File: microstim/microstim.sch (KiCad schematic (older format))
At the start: 89 parts, among them J1 Conn_Coaxial, J10 Conn_Coaxial, J11 Screw_Terminal_01x02, J12 Conn_Coaxial, J3 Screw_Terminal_01x02, J5 Conn_Coaxial, J7 Screw_Terminal_01x02, J9 Screw_Terminal_01x02, SW1 SW_Push, SW2 SW_Push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

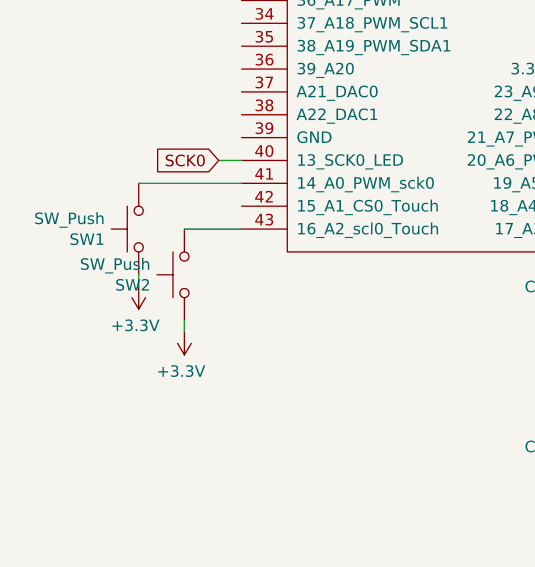
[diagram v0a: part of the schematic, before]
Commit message: added datasheets for connector and enclosure. updated BOM. probably tons of updates to schematic/layout (cant remember when last commit was). layout/schematic complete - just need double-checking.
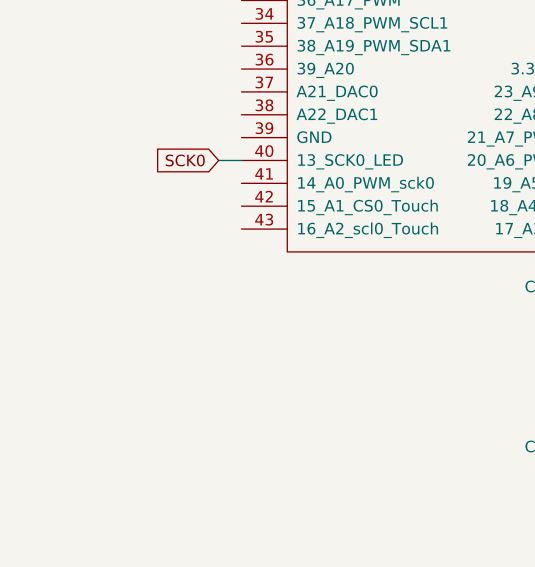
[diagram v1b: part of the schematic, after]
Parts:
- removed SW1, SW2: SW_Push, Button_Switch_SMD:SW_SPST_PTS645, symbol Switch:SW_Push
- J1, J10, J12, J5: footprint Connector_Coaxial:SMA_Amphenol_901-144_Vertical -> microstim:731375003
- J11, J3, J7, J9: footprint TerminalBlock_4Ucon:TerminalBlock_4Ucon_1x02_P3.50mm_Vertical -> microstim:1-2834016-2 _TERM_BLK_2P_SIDE_ENT_2.54MM_PCB
- U1: footprint microstim:Teensy35_36 -> microstim:Teensy35_36_noInternalPins
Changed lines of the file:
@@
 F 0 "U1" H 2150 5687 60  0000 C CNN
 F 1 "Teensy3.5" H 2150 5581 60  0000 C CNN
-F 2 "microstim:Teensy35_36" H 2150 3300 60  0001 C CNN
+F 2 "microstim:Teensy35_36_noInternalPins" H 2150 3300 60  0001 C CNN
 F 3 "" H 2150 3300 60  0000 C CNN
 	1    2150 3300
@@
 F 0 "J1" H 2480 6038 50  0000 C CNN
 F 1 "Conn_Coaxial" H 2480 5947 50  0000 C CNN
-F 2 "Connector_Coaxial:SMA_Amphenol_901-144_Vertical" H 2550 5800 50  0001 C CNN
+F 2 "microstim:731375003" H 2550 5800 50  0001 C CNN
 F 3 " ~" H 2550 5800 50  0001 C CNN
 	1    2550 5800
@@
 F 0 "J3" H 2820 6017 50  0000 C CNN
 F 1 "Screw_Terminal_01x02" H 2820 5926 50  0000 C CNN
-F 2 "TerminalBlock_4Ucon:TerminalBlock_4Ucon_1x02_P3.50mm_Vertical" H 2900 5800 50  0001 C CNN
+F 2 "microstim:1-2834016-2 _TERM_BLK_2P_SIDE_ENT_2.54MM_PCB" H 2900 5800 50  0001 C CNN
 F 3 "~" H 2900 5800 50  0001 C CNN
 	1    2900 5800
@@
 F 0 "J5" H 2480 6738 50  0000 C CNN
 F 1 "Conn_Coaxial" H 2480 6647 50  0000 C CNN
-F 2 "Connector_Coaxial:SMA_Amphenol_901-144_Vertical" H 2550 6500 50  0001 C CNN
+F 2 "microstim:731375003" H 2550 6500 50  0001 C CNN
 F 3 " ~" H 2550 6500 50  0001 C CNN
 	1    2550 6500
@@
 F 0 "J7" H 2820 6717 50  0000 C CNN
 F 1 "Screw_Terminal_01x02" H 2820 6626 50  0000 C CNN
-F 2 "TerminalBlock_4Ucon:TerminalBlock_4Ucon_1x02_P3.50mm_Vertical" H 2900 6500 50  0001 C CNN
+F 2 "microstim:1-2834016-2 _TERM_BLK_2P_SIDE_ENT_2.54MM_PCB" H 2900 6500 50  0001 C CNN
 F 3 "~" H 2900 6500 50  0001 C CNN
 	1    2900 6500
@@
 Wire Wire Line
 	3300 6400 3300 6500
-$Comp
-L Switch:SW_Push SW1
-U 1 1 5B7C9AA6
-P 700 5400
-F 0 "SW1" V 654 5548 50  0000 L CNN
-F 1 "SW_Push" V 745 5548 50  0000 L CNN
-F 2 "Button_Switch_SMD:SW_SPST_PTS645" H 700 5600 50  0001 C CNN
-F 3 "" H 700 5600 50  0001 C CNN
-	1    700  5400
-	0    -1   -1   0
-$EndComp
-$Comp
-L Switch:SW_Push SW2
-U 1 1 5B7C9D93
-P 900 5600
-F 0 "SW2" V 854 5748 50  0000 L CNN
-F 1 "SW_Push" V 945 5748 50  0000 L CNN
-F 2 "Button_Switch_SMD:SW_SPST_PTS645" H 900 5800 50  0001 C CNN
-F 3 "" H 900 5800 50  0001 C CNN
-	1    900  5600
-	0    -1   -1   0
-$EndComp
 $Comp
 L power:GND #PWR018
@@
 	1    0    0    -1
 $EndComp
-$Comp
-L power:+3.3V #PWR01
-U 1 1 5B7D4ED6
-P 700 5650
-F 0 "#PWR01" H 700 5500 50  0001 C CNN
-F 1 "+3.3V" H 715 5823 50  0000 C CNN
-F 2 "" H 700 5650 50  0001 C CNN
-F 3 "" H 700 5650 50  0001 C CNN
-	1    700  5650
-	-1   0    0    1
-$EndComp
-$Comp
-L power:+3.3V #PWR02
-U 1 1 5B7D4F09
-P 900 5850
-F 0 "#PWR02" H 900 5700 50  0001 C CNN
-F 1 "+3.3V" H 915 6023 50  0000 C CNN
-F 2 "" H 900 5850 50  0001 C CNN
-F 3 "" H 900 5850 50  0001 C CNN
-	1    900  5850
-	-1   0    0    1
-$EndComp
-Wire Wire Line
-	700  5600 700  5650
-Wire Wire Line
-	900  5800 900  5850
 $Comp
 L Device:R_US R3
@@
 F 0 "J12" H 15630 6038 50  0000 C CNN
 F 1 "Conn_Coaxial" H 15630 5947 50  0000 C CNN
-F 2 "Connector_Coaxial:SMA_Amphenol_901-144_Vertical" H 15700 5800 50  0001 C CNN
+F 2 "microstim:731375003" H 15700 5800 50  0001 C CNN
 F 3 " ~" H 15700 5800 50  0001 C CNN
 	1    15700 5800
@@
 F 0 "J11" H 15270 6017 50  0000 C CNN
 F 1 "Screw_Terminal_01x02" H 15270 5926 50  0000 C CNN
-F 2 "TerminalBlock_4Ucon:TerminalBlock_4Ucon_1x02_P3.50mm_Vertical" H 15350 5800 50  0001 C CNN
+F 2 "microstim:1-2834016-2 _TERM_BLK_2P_SIDE_ENT_2.54MM_PCB" H 15350 5800 50  0001 C CNN
 F 3 "~" H 15350 5800 50  0001 C CNN
 	1    15350 5800
@@
 F 0 "J10" H 15730 2738 50  0000 C CNN
 F 1 "Conn_Coaxial" H 15730 2647 50  0000 C CNN
-F 2 "Connector_Coaxial:SMA_Amphenol_901-144_Vertical" H 15800 2500 50  0001 C CNN
+F 2 "microstim:731375003" H 15800 2500 50  0001 C CNN
 F 3 " ~" H 15800 2500 50  0001 C CNN
 	1    15800 2500
@@
 F 0 "J9" H 15370 2717 50  0000 C CNN
 F 1 "Screw_Terminal_01x02" H 15370 2626 50  0000 C CNN
-F 2 "TerminalBlock_4Ucon:TerminalBlock_4Ucon_1x02_P3.50mm_Vertical" H 15450 2500 50  0001 C CNN
+F 2 "microstim:1-2834016-2 _TERM_BLK_2P_SIDE_ENT_2.54MM_PCB" H 15450 2500 50  0001 C CNN
 F 3 "~" H 15450 2500 50  0001 C CNN
 	1    15450 2500
@@
 Wire Wire Line
 	5250 2100 5350 2100
-Wire Wire Line
-	700  5200 1150 5200
-Wire Wire Line
-	1150 5400 900  5400
 $Comp
 L power:+3.3V #PWR0103

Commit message: fixed logic bug and added explicit logic table to schematic
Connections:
- net +5V: now also C11.1; no longer C11.2
- net GNDREF: now also C11.2, U16.10 (S4B), U18.10 (S4B); no longer C11.1, U16.13 (S1B), U18.13 (S1B)
- net VOUT0: now also U18.13 (S1B); no longer U18.11 (S3B)
- net VOUT1: now also U16.13 (S1B); no longer U16.11 (S3B)
- net at U18.7 (S4A): now also R13.1, U18.4 (S1A); no longer U18.10 (S4B)
- net at U16.7 (S4A): now also R9.2, U16.4 (S1A); no longer U16.10 (S4B)
- new net: U18.11 (S3B), U18.6 (S3A)
- new net: U16.11 (S3B), U16.6 (S3A)
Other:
- note added: "OE0 OE1 Output Input (ADC)\n\n 0 0 VOLTAGE OUT0\n 1 0 CURRENT OUT0\n 0 1 CURRENT ISENSE0\n 1 1 GND ISENSE0"
- moved on the sheet: C11, C13, C17, C19, C24, C25, C3, C36, C40, C5, C9, H1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
